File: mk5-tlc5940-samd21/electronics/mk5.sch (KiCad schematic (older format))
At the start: 55 parts, among them J1 IN/OUT, J10 3, J11 4, J12 5, J13 6, J14 7, J15 8, J16 9, J17 10, J18 11, J19 12, J2 USB, J20 13, J21 14, J22 15, J23 +LED, J24 +LED, J25 +LED, J26 +LED, J27 +LED, J28 Button, J29 GND, J3 15S, J4 GS2, J5 +3V3, J6 +LED, J7 0, J8 1, J9 2, Q1 MOSFET 20V 3A, SW1 BTN, U2 MCP1702-3302_SOT23, U3 SAMD21E15A-MU, U4 TLC5940PWP

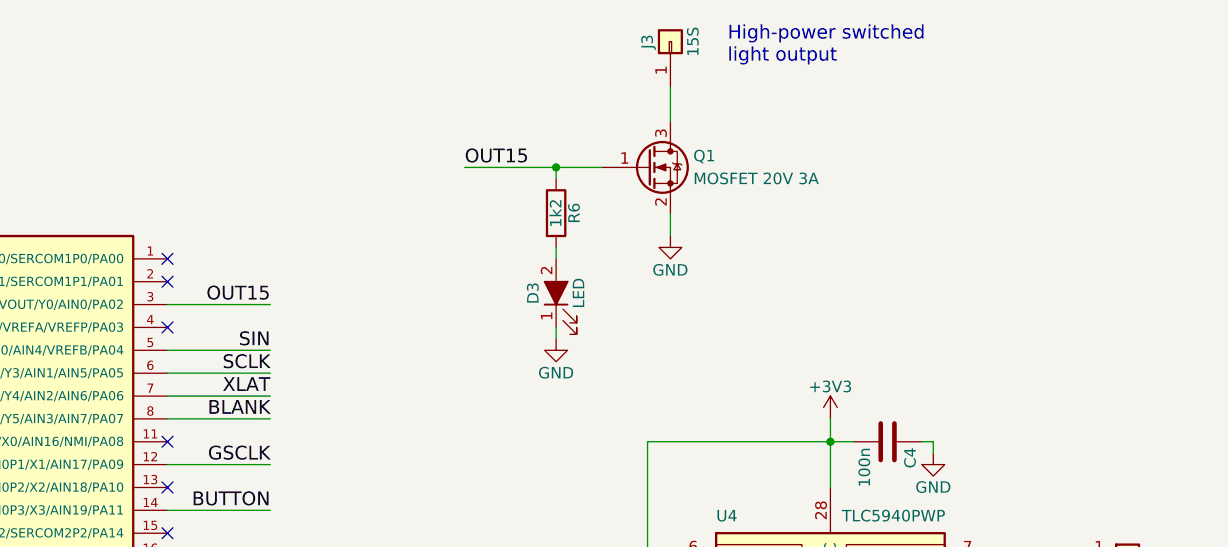
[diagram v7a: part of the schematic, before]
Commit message: LED is separate from OUT15
We put it on PA01, which is one of the crystal pin on Arduino.
On Arduino the LED is on PB08, which we don't have on the
32 pin package.
We will have to see if we can drive two LEDs with the same software,
especially in the boot loader
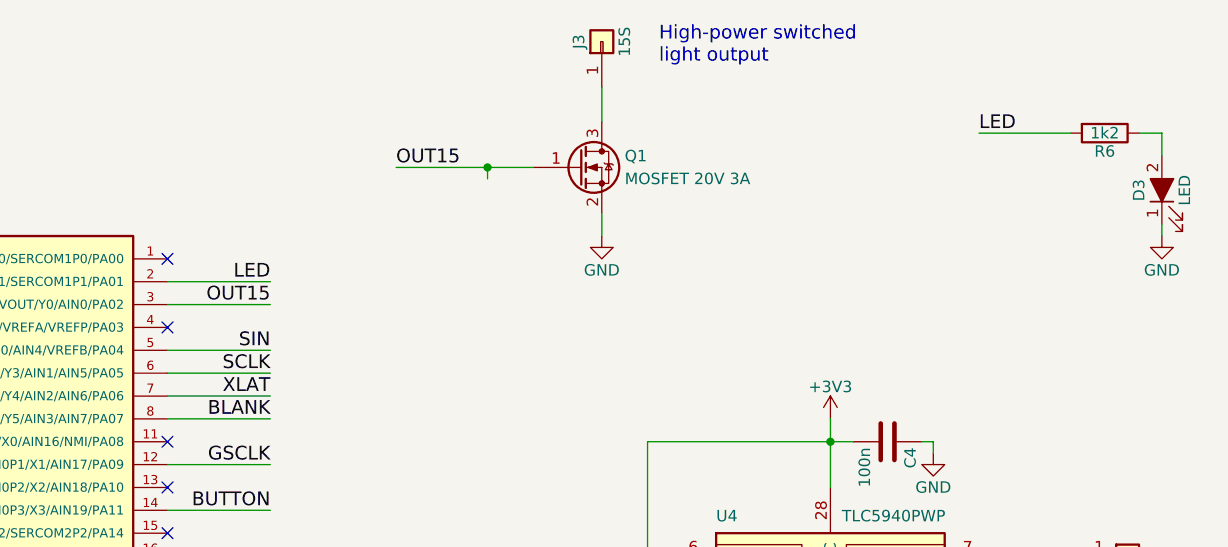
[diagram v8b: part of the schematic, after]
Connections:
- net OUT15: no longer R6.1
- net at D3.2 (A): now also R6.1; no longer R6.2
- net LED: now reaches U3.2 (XOUT32/TC2WO1/SERCOM1P1/PA01)
- net LED: now also R6.2
- no-connect marks 17 -> 16
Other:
- moved on the sheet: D3, J3, Q1, R6
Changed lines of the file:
@@
 L GND #PWR05
 U 1 1 59C46A64
-P 8550 1550
-F 0 "#PWR05" H 8550 1300 50  0001 C CNN
-F 1 "GND" H 8550 1400 50  0000 C CNN
-F 2 "" H 8550 1550 50  0001 C CNN
-F 3 "" H 8550 1550 50  0001 C CNN
-	1    8550 1550
+P 8250 1550
+F 0 "#PWR05" H 8250 1300 50  0001 C CNN
+F 1 "GND" H 8250 1400 50  0000 C CNN
+F 2 "" H 8250 1550 50  0001 C CNN
+F 3 "" H 8250 1550 50  0001 C CNN
+	1    8250 1550
 	1    0    0    -1
 $EndComp
@@
 L Conn_01x01 J3
 U 1 1 59C4821D
-P 8550 700
-F 0 "J3" H 8550 800 50  0000 C CNN
-F 1 "15S" H 8550 600 50  0000 C CNN
-F 2 "SMD-pads:SMD50x100" H 8550 700 50  0001 C CNN
-F 3 "" H 8550 700 50  0001 C CNN
-	1    8550 700
+P 8250 700
+F 0 "J3" H 8250 800 50  0000 C CNN
+F 1 "15S" H 8250 600 50  0000 C CNN
+F 2 "SMD-pads:SMD50x100" H 8250 700 50  0001 C CNN
+F 3 "" H 8250 700 50  0001 C CNN
+	1    8250 700
 	0    -1   -1   0
 $EndComp
@@
 L Q_NMOS_GSD Q1
 U 1 1 59C4D834
-P 8450 1250
-F 0 "Q1" H 8650 1300 50  0000 L CNN
-F 1 "MOSFET 20V 3A" H 8650 1200 50  0000 L CNN
-F 2 "TO_SOT_Packages_SMD:SOT-23" H 8650 1350 50  0001 C CNN
-F 3 "" H 8450 1250 50  0001 C CNN
-	1    8450 1250
+P 8150 1250
+F 0 "Q1" H 8350 1300 50  0000 L CNN
+F 1 "MOSFET 20V 3A" H 8350 1200 50  0000 L CNN
+F 2 "TO_SOT_Packages_SMD:SOT-23" H 8350 1350 50  0001 C CNN
+F 3 "" H 8150 1250 50  0001 C CNN
+	1    8150 1250
 	1    0    0    -1
 $EndComp
@@
 L LED_ALT D3
 U 1 1 59DC7006
-P 8050 1800
-F 0 "D3" H 8050 1900 50  0000 C CNN
-F 1 "LED" H 8050 1700 50  0000 C CNN
-F 2 "LEDs:LED_0603" H 8050 1800 50  0001 C CNN
-F 3 "" H 8050 1800 50  0001 C CNN
-	1    8050 1800
+P 10700 1350
+F 0 "D3" H 10700 1450 50  0000 C CNN
+F 1 "LED" H 10700 1250 50  0000 C CNN
+F 2 "LEDs:LED_0603" H 10700 1350 50  0001 C CNN
+F 3 "" H 10700 1350 50  0001 C CNN
+	1    10700 1350
 	0    -1   -1   0
 $EndComp
@@
 L R R6
 U 1 1 59DC70B5
-P 8050 1450
-F 0 "R6" V 8130 1450 50  0000 C CNN
-F 1 "1k2" V 8050 1450 50  0000 C CNN
-F 2 "Resistors_SMD:R_0603" V 7980 1450 50  0001 C CNN
-F 3 "" H 8050 1450 50  0001 C CNN
-	1    8050 1450
-	1    0    0    -1
+P 10450 1100
+F 0 "R6" V 10530 1100 50  0000 C CNN
+F 1 "1k2" V 10450 1100 50  0000 C CNN
+F 2 "Resistors_SMD:R_0603" V 10380 1100 50  0001 C CNN
+F 3 "" H 10450 1100 50  0001 C CNN
+	1    10450 1100
+	0    1    1    0
 $EndComp
 $Comp
 L GND #PWR023
 U 1 1 59DC74AB
-P 8050 2000
-F 0 "#PWR023" H 8050 1750 50  0001 C CNN
-F 1 "GND" H 8050 1850 50  0000 C CNN
-F 2 "" H 8050 2000 50  0001 C CNN
-F 3 "" H 8050 2000 50  0001 C CNN
-	1    8050 2000
+P 10700 1550
+F 0 "#PWR023" H 10700 1300 50  0001 C CNN
+F 1 "GND" H 10700 1400 50  0000 C CNN
+F 2 "" H 10700 1550 50  0001 C CNN
+F 3 "" H 10700 1550 50  0001 C CNN
+	1    10700 1550
 	1    0    0    -1
 $EndComp
@@
 Text Label 8150 4350 0    60   ~ 0
 SIN
-Text Label 7650 1250 0    60   ~ 0
+Text Label 7350 1250 0    60   ~ 0
 OUT15
 $Comp
@@
 	6350 3750 6800 3750
 Wire Wire Line
-	8550 1450 8550 1550
-Wire Wire Line
-	8550 900  8550 1050
+	8250 1450 8250 1550
+Wire Wire Line
+	8250 900  8250 1050
 Wire Wire Line
 	8450 2450 9350 2450
@@
 	1850 1100 1850 1750
 Wire Wire Line
-	7650 1250 8250 1250
+	7350 1250 7950 1250
 Wire Wire Line
 	1400 1650 2300 1650
@@
 	1850 1750 1400 1750
 Wire Wire Line
-	8050 1600 8050 1650
-Wire Wire Line
-	8050 1950 8050 2000
+	10700 1100 10700 1200
+Wire Wire Line
+	10700 1500 10700 1550
 Wire Wire Line
 	1850 2100 1850 2150
@@
 	5900 5600 5450 5600
 Wire Wire Line
-	8050 1300 8050 1250
-Connection ~ 8050 1250
+	7750 1300 7750 1250
+Connection ~ 7750 1250
 Wire Wire Line
 	1450 7000 2300 7000
@@
 	1    0    0    -1
 $EndComp
-Text Notes 8800 800  0    60   ~ 0
+Text Notes 8500 800  0    60   ~ 0
 High-power switched\nlight output
 Wire Wire Line
@@
 	6350 3350 6800 3350
 NoConn ~ 6350 1650
-NoConn ~ 6350 1750
 NoConn ~ 6350 2850
 NoConn ~ 6350 3850
@@
 	6350 1850 6800 1850
 NoConn ~ 6350 1950
+Wire Wire Line
+	10600 1100 10700 1100
+Wire Wire Line
+	10300 1100 9900 1100
+Text Label 9900 1100 0    60   ~ 0
+LED
+Wire Wire Line
+	6350 1750 6800 1750
+Text Label 6800 1750 2    60   ~ 0
+LED
 $EndSCHEMATC
